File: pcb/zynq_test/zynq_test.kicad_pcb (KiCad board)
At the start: 2 copper layers, 1 part, among them U1 XC7Z020-2CLG400I

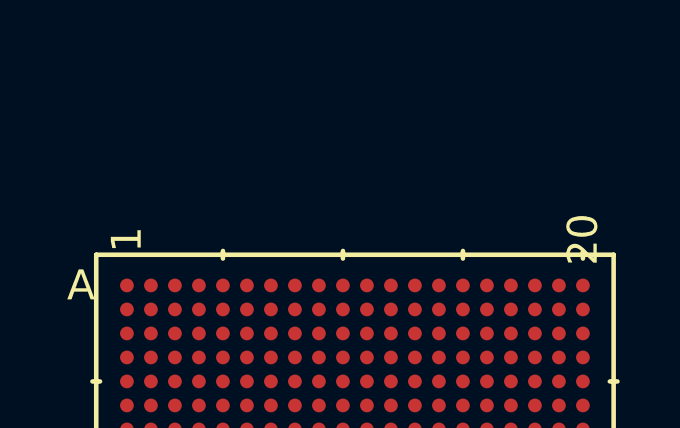
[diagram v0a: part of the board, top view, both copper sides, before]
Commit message: Changed MIO signals to Buses
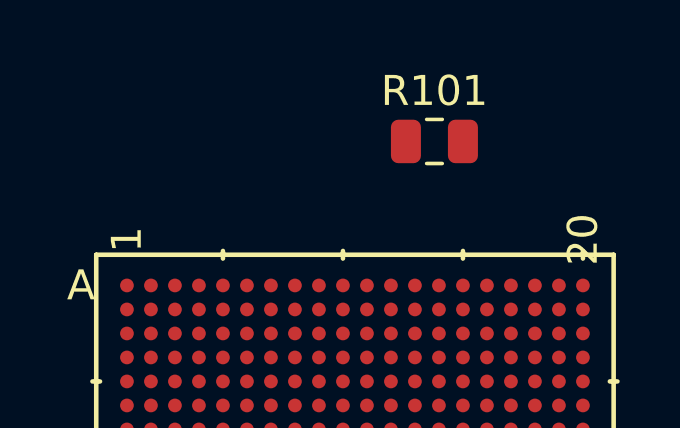
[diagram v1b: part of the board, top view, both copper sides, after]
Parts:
- added R101: R, Capacitor_SMD:C_0805_2012Metric, F.Cu at (137.6, 107.0)
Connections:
- net ETH0-MDC renamed /zynqMio/ETH0-MDC
- net ETH0-MDIO renamed /zynqMio/ETH0-MDIO
- net ETH0-RX-CLK renamed /zynqMio/ETH0-RX-CLK
- net ETH0-RX-CTL renamed /zynqMio/ETH0-RX-CTL
- net ETH0-RXD-0 renamed /zynqMio/ETH0-RXD-0
- net ETH0-RXD-1 renamed /zynqMio/ETH0-RXD-1
- net ETH0-RXD-2 renamed /zynqMio/ETH0-RXD-2
- net ETH0-RXD-3 renamed /zynqMio/ETH0-RXD-3
- net ETH0-TX-CLK renamed /zynqMio/ETH0-TX-CLK
- net ETH0-TX-CTL renamed /zynqMio/ETH0-TX-CTL
- net ETH0-TXD-0 renamed /zynqMio/ETH0-TXD-0
- net ETH0-TXD-1 renamed /zynqMio/ETH0-TXD-1
- net ETH0-TXD-2 renamed /zynqMio/ETH0-TXD-2
- net ETH0-TXD-3 renamed /zynqMio/ETH0-TXD-3
- net MIO0-2 renamed MIO0-8
- net MIO0-3 renamed MIO0-9
- net MIO0-4 renamed MIO0-10
- net MIO0-5 renamed MIO0-11
- net MIO0-6 renamed MIO0-12
- net MIO1-0 renamed /zynqMio/MIO1-46
- net MIO1-1 renamed /zynqMio/MIO1-47
- net MIO1-2 renamed /zynqMio/MIO1-48
- net MIO1-3 renamed /zynqMio/MIO1-49
- net MIO1-4 renamed /zynqMio/MIO1-50
- net MIO1-5 renamed /zynqMio/MIO1-51
- net QSPI0-IO-0/MODE-0 renamed QSPI0-IO-0
- net QSPI0-IO-1/MODE-1 renamed QSPI0-IO-1
- net QSPI0-IO-2/MODE-2 renamed QSPI0-IO-2
- net QSPI0-IO-3/MODE-3 renamed QSPI0-IO-3
- net QSPI0-SCLK/MODE-4 renamed QSPI0-SCLK
- net SD0-CLK renamed /zynqMio/SD0-CLK
- net SD0-CMD renamed /zynqMio/SD0-CMD
- net SD0-DATA-0 renamed /zynqMio/SD0-DATA-0
- net SD0-DATA-1 renamed /zynqMio/SD0-DATA-1
- net SD0-DATA-2 renamed /zynqMio/SD0-DATA-2
- net SD0-DATA-3 renamed /zynqMio/SD0-DATA-3
- net USB0-CLK renamed /zynqMio/USB0-CLK
- net USB0-DATA-0 renamed /zynqMio/USB0-DATA-0
- net USB0-DATA-1 renamed /zynqMio/USB0-DATA-1
- net USB0-DATA-2 renamed /zynqMio/USB0-DATA-2
- net USB0-DATA-3 renamed /zynqMio/USB0-DATA-3
- net USB0-DATA-4 renamed /zynqMio/USB0-DATA-4
- net USB0-DATA-5 renamed /zynqMio/USB0-DATA-5
- net USB0-DATA-6 renamed /zynqMio/USB0-DATA-6
- net USB0-DATA-7 renamed /zynqMio/USB0-DATA-7
- net USB0-DIR renamed /zynqMio/USB0-DIR
- net USB0-NXT renamed /zynqMio/USB0-NXT
- net USB0-STP renamed /zynqMio/USB0-STP
- U1 pad D8: MIO0-1 -> MIO0-7
- U1 pad E11: unconnected-(U1F-PS_MIO_VREF_501-PadE11) -> /zynqMio/0.9_Vref
- U1 pad E8: MIO0-7 -> MIO0-13

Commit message: Finished PS, started on PWR
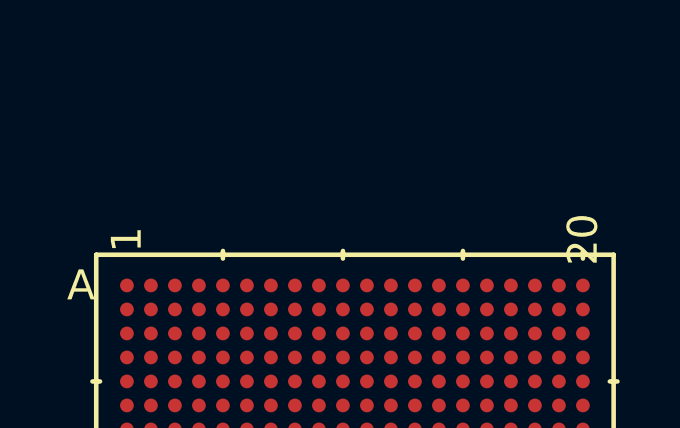
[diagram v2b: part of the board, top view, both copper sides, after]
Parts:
- removed R101: R, Capacitor_SMD:C_0805_2012Metric
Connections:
- net /zynqMio/CLK-33.33M renamed /zynqMio/PS-CLK-33.33M
- net /zynqMio/ETH0-MDC renamed /zynqMio/ETH0.MDC
- net /zynqMio/ETH0-MDIO renamed /zynqMio/ETH0.MDIO
- net /zynqMio/ETH0-RX-CLK renamed /zynqMio/ETH0.RX-CLK
- net /zynqMio/ETH0-RX-CTL renamed /zynqMio/ETH0.RX-CTL
- net /zynqMio/ETH0-RXD-0 renamed /zynqMio/ETH0.RXD-0
- net /zynqMio/ETH0-RXD-1 renamed /zynqMio/ETH0.RXD-1
- net /zynqMio/ETH0-RXD-2 renamed /zynqMio/ETH0.RXD-2
- net /zynqMio/ETH0-RXD-3 renamed /zynqMio/ETH0.RXD-3
- net /zynqMio/ETH0-TX-CLK renamed /zynqMio/ETH0.TX-CLK.Z
- net /zynqMio/ETH0-TX-CTL renamed /zynqMio/ETH0.TX-CTL
- net /zynqMio/ETH0-TXD-0 renamed /zynqMio/ETH0.TXD-0.Z
- net /zynqMio/ETH0-TXD-1 renamed /zynqMio/ETH0.TXD-1.Z
- net /zynqMio/ETH0-TXD-2 renamed /zynqMio/ETH0.TXD-2.Z
- net /zynqMio/ETH0-TXD-3 renamed /zynqMio/ETH0.TXD-3.Z
- net /zynqMio/MIO1-46 renamed /zynqMio/MIO1.46
- net /zynqMio/MIO1-47 renamed /zynqMio/MIO1.47
- net /zynqMio/MIO1-48 renamed /zynqMio/MIO1.48
- net /zynqMio/MIO1-49 renamed /zynqMio/MIO1.49
- net /zynqMio/MIO1-50 renamed /zynqMio/MIO1.50
- net /zynqMio/MIO1-51 renamed /zynqMio/MIO1.51
- net /zynqMio/SD0-CLK renamed /zynqMio/SD0.CLK
- net /zynqMio/SD0-CMD renamed /zynqMio/SD0.CMD
- net /zynqMio/SD0-DATA-0 renamed /zynqMio/SD0.DATA-0
- net /zynqMio/SD0-DATA-1 renamed /zynqMio/SD0.DATA-1
- net /zynqMio/SD0-DATA-2 renamed /zynqMio/SD0.DATA-2
- net /zynqMio/SD0-DATA-3 renamed /zynqMio/SD0.DATA-3
- net /zynqMio/USB0-CLK renamed /zynqMio/USB0.CLK
- net /zynqMio/USB0-DATA-0 renamed /zynqMio/USB0.DATA-0
- net /zynqMio/USB0-DATA-1 renamed /zynqMio/USB0.DATA-1
- net /zynqMio/USB0-DATA-2 renamed /zynqMio/USB0.DATA-2
- net /zynqMio/USB0-DATA-3 renamed /zynqMio/USB0.DATA-3
- net /zynqMio/USB0-DATA-4 renamed /zynqMio/USB0.DATA-4
- net /zynqMio/USB0-DATA-5 renamed /zynqMio/USB0.DATA-5
- net /zynqMio/USB0-DATA-6 renamed /zynqMio/USB0.DATA-6
- net /zynqMio/USB0-DATA-7 renamed /zynqMio/USB0.DATA-7
- net /zynqMio/USB0-DIR renamed /zynqMio/USB0.DIR
- net /zynqMio/USB0-NXT renamed /zynqMio/USB0.NXT
- net /zynqMio/USB0-STP renamed /zynqMio/USB0.STP
- net MIO0-0 renamed /zynqMio/MIO0.0
- net MIO0-10 renamed /zynqMio/MIO0.10
- net MIO0-11 renamed /zynqMio/MIO0.11
- net MIO0-12 renamed /zynqMio/MIO0.12
- net MIO0-13 renamed /zynqMio/MIO0.13
- net MIO0-7 renamed /zynqMio/MIO0.7
- net MIO0-8 renamed /zynqMio/MIO0.8
- net MIO0-9 renamed /zynqMio/MIO0.9
- net QSPI0-IO-0 renamed /zynqMio/QSPI0.IO-0
- net QSPI0-IO-1 renamed /zynqMio/QSPI0.IO-1
- net QSPI0-IO-2 renamed /zynqMio/QSPI0.IO-2
- net QSPI0-IO-3 renamed /zynqMio/QSPI0.IO-3
- net QSPI0-SCLK renamed /zynqMio/QSPI0.SCLK.Z
- net QSPI0-SS-B renamed /zynqMio/QSPI0.SS-B
- net UART0-RX renamed /zynqMio/UART0.RX
- net UART0-TX renamed /zynqMio/UART0.TX
- U1 pad A18: unconnected-(U1H-GND-PadA18) -> GND
- U1 pad A8: unconnected-(U1H-GND-PadA8) -> GND
- U1 pad B1: unconnected-(U1H-GND-PadB1) -> GND
- U1 pad B10: (no net) -> unconnected-(U1A-PS_SRST_B_501-PadB10)
- U1 pad B11: unconnected-(U1H-GND-PadB11) -> GND
- U1 pad C14: unconnected-(U1H-GND-PadC14) -> GND
- U1 pad C4: unconnected-(U1H-GND-PadC4) -> GND
- U1 pad C7: (no net) -> unconnected-(U1A-PS_POR_B_500-PadC7)
- U1 pad C9: unconnected-(U1H-GND-PadC9) -> GND
- U1 pad D17: unconnected-(U1H-GND-PadD17) -> GND
- U1 pad E10: unconnected-(U1H-GND-PadE10) -> GND
- U1 pad E20: unconnected-(U1H-GND-PadE20) -> GND
- U1 pad F11: unconnected-(U1A-VCCBATT_0-PadF11) -> GND
- U1 pad F3: unconnected-(U1H-GND-PadF3) -> GND
- U1 pad F7: unconnected-(U1H-GND-PadF7) -> GND
- U1 pad F8: unconnected-(U1H-VCCPAUX-PadF8) -> Net-(C519-Pad1)
- U1 pad G10: unconnected-(U1H-GND-PadG10) -> GND
- U1 pad G11: unconnected-(U1H-VCCBRAM-PadG11) -> Net-(C508-Pad1)
- U1 pad G12: unconnected-(U1H-GND-PadG12) -> GND
- U1 pad G13: unconnected-(U1H-VCCINT-PadG13) -> Net-(C501-Pad1)
- U1 pad G16: unconnected-(U1H-GND-PadG16) -> GND
- U1 pad G7: unconnected-(U1H-VCCPINT-PadG7) -> Net-(C514-Pad1)
- U1 pad G8: unconnected-(U1H-VCCPLL-PadG8) -> Net-(U1H-VCCPLL)
- U1 pad G9: unconnected-(U1H-VCCPAUX-PadG9) -> Net-(C519-Pad1)
- U1 pad H10: unconnected-(U1H-VCCBRAM-PadH10) -> Net-(C508-Pad1)
- U1 pad H11: unconnected-(U1H-GND-PadH11) -> GND
- U1 pad H12: unconnected-(U1H-VCCINT-PadH12) -> Net-(C501-Pad1)
- U1 pad H13: unconnected-(U1H-GND-PadH13) -> GND
- U1 pad H19: unconnected-(U1H-GND-PadH19) -> GND
- U1 pad H7: unconnected-(U1H-GND-PadH7) -> GND
- U1 pad H8: unconnected-(U1H-VCCPAUX-PadH8) -> Net-(C519-Pad1)
- U1 pad H9: unconnected-(U1H-GND-PadH9) -> GND
- U1 pad J11: unconnected-(U1H-VCCAUX-PadJ11) -> Net-(C511-Pad1)
- U1 pad J12: unconnected-(U1H-GND-PadJ12) -> GND
- U1 pad J13: unconnected-(U1H-VCCINT-PadJ13) -> Net-(C501-Pad1)
- U1 pad J2: unconnected-(U1H-GND-PadJ2) -> GND
- U1 pad J7: unconnected-(U1H-VCCPINT-PadJ7) -> Net-(C514-Pad1)
- U1 pad J8: unconnected-(U1H-GND-PadJ8) -> GND
- U1 pad K11: unconnected-(U1H-GND-PadK11) -> GND
- U1 pad K12: unconnected-(U1H-VCCINT-PadK12) -> Net-(C501-Pad1)
- U1 pad K13: unconnected-(U1H-GND-PadK13) -> GND
- U1 pad K15: unconnected-(U1H-GND-PadK15) -> GND
- U1 pad K5: unconnected-(U1H-GND-PadK5) -> GND
- U1 pad K6: unconnected-(U1A-VCCO_0-PadK6) -> Net-(U1H-VCCO_0)
- U1 pad K7: unconnected-(U1H-GND-PadK7) -> GND
- U1 pad K8: unconnected-(U1H-VCCPAUX-PadK8) -> Net-(C519-Pad1)
- U1 pad L11: unconnected-(U1H-VCCAUX-PadL11) -> Net-(C511-Pad1)
- U1 pad L12: unconnected-(U1H-GND-PadL12) -> GND
- U1 pad L13: unconnected-(U1H-VCCINT-PadL13) -> Net-(C501-Pad1)
- U1 pad L18: unconnected-(U1H-GND-PadL18) -> GND
- U1 pad L7: unconnected-(U1H-VCCPINT-PadL7) -> Net-(C514-Pad1)
- U1 pad L8: unconnected-(U1H-GND-PadL8) -> GND
- U1 pad M1: unconnected-(U1H-GND-PadM1) -> GND
- U1 pad M11: unconnected-(U1H-GND-PadM11) -> GND
- U1 pad M12: unconnected-(U1H-VCCINT-PadM12) -> Net-(C501-Pad1)
- U1 pad M13: unconnected-(U1H-GND-PadM13) -> GND
- U1 pad M7: unconnected-(U1H-GND-PadM7) -> GND
- U1 pad M8: unconnected-(U1H-VCCPAUX-PadM8) -> Net-(C519-Pad1)
- U1 pad N10: unconnected-(U1H-GND-PadN10) -> GND
- U1 pad N11: unconnected-(U1H-VCCAUX-PadN11) -> Net-(C511-Pad1)
- U1 pad N12: unconnected-(U1H-GND-PadN12) -> GND
- U1 pad N13: unconnected-(U1H-VCCINT-PadN13) -> Net-(C501-Pad1)
- U1 pad N14: unconnected-(U1H-GND-PadN14) -> GND
- U1 pad N4: unconnected-(U1H-GND-PadN4) -> GND
- U1 pad N7: unconnected-(U1H-VCCPINT-PadN7) -> Net-(C514-Pad1)
- U1 pad N8: unconnected-(U1H-GND-PadN8) -> GND
- U1 pad N9: unconnected-(U1H-VCCAUX-PadN9) -> Net-(C511-Pad1)
- U1 pad P10: unconnected-(U1H-VCCAUX-PadP10) -> Net-(C511-Pad1)
- U1 pad P11: unconnected-(U1H-GND-PadP11) -> GND
- U1 pad P12: unconnected-(U1H-VCCINT-PadP12) -> Net-(C501-Pad1)
- U1 pad P13: unconnected-(U1H-GND-PadP13) -> GND
- U1 pad P17: unconnected-(U1H-GND-PadP17) -> GND
- U1 pad P7: unconnected-(U1H-GND-PadP7) -> GND
- U1 pad P8: unconnected-(U1H-VCCPINT-PadP8) -> Net-(C514-Pad1)
- U1 pad P9: unconnected-(U1H-GND-PadP9) -> GND
- U1 pad R12: unconnected-(U1H-GND-PadR12) -> GND
- U1 pad R13: unconnected-(U1H-VCCINT-PadR13) -> Net-(C501-Pad1)
- U1 pad R20: unconnected-(U1H-GND-PadR20) -> GND
- U1 pad R7: unconnected-(U1H-VCCPINT-PadR7) -> Net-(C514-Pad1)
- U1 pad R8: unconnected-(U1H-GND-PadR8) -> GND
- U1 pad R9: unconnected-(U1H-VCCAUX-PadR9) -> Net-(C511-Pad1)
- U1 pad T13: unconnected-(U1H-GND-PadT13) -> GND
- U1 pad T3: unconnected-(U1H-GND-PadT3) -> GND
- U1 pad T7: unconnected-(U1H-GND-PadT7) -> GND
- U1 pad U16: unconnected-(U1H-GND-PadU16) -> GND
- U1 pad U6: unconnected-(U1H-GND-PadU6) -> GND
- U1 pad V19: unconnected-(U1H-GND-PadV19) -> GND
- U1 pad V9: unconnected-(U1H-GND-PadV9) -> GND
- U1 pad W12: unconnected-(U1H-GND-PadW12) -> GND
- U1 pad W2: unconnected-(U1H-GND-PadW2) -> GND
- U1 pad Y15: unconnected-(U1H-GND-PadY15) -> GND
- U1 pad Y5: unconnected-(U1H-GND-PadY5) -> GND

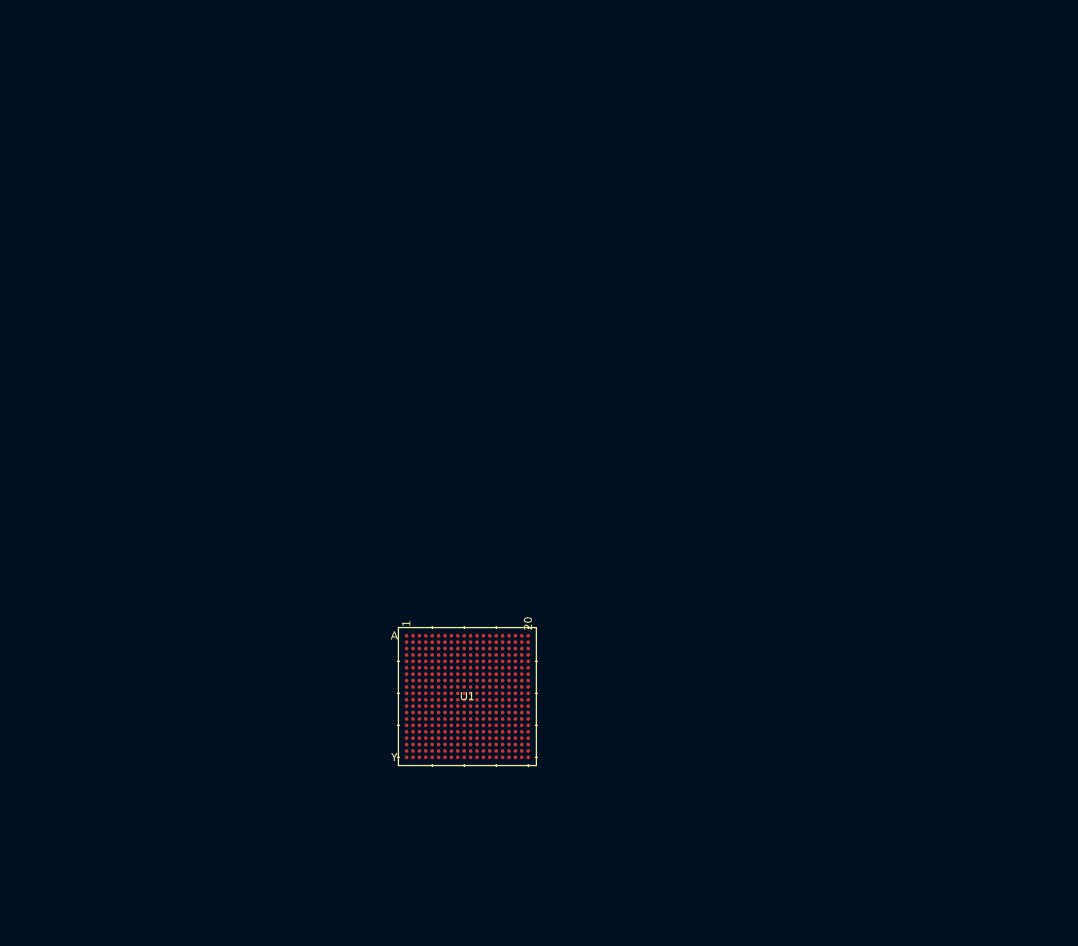
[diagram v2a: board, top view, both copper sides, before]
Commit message: Finished Ethernet, swapped FTDI chip for QFN
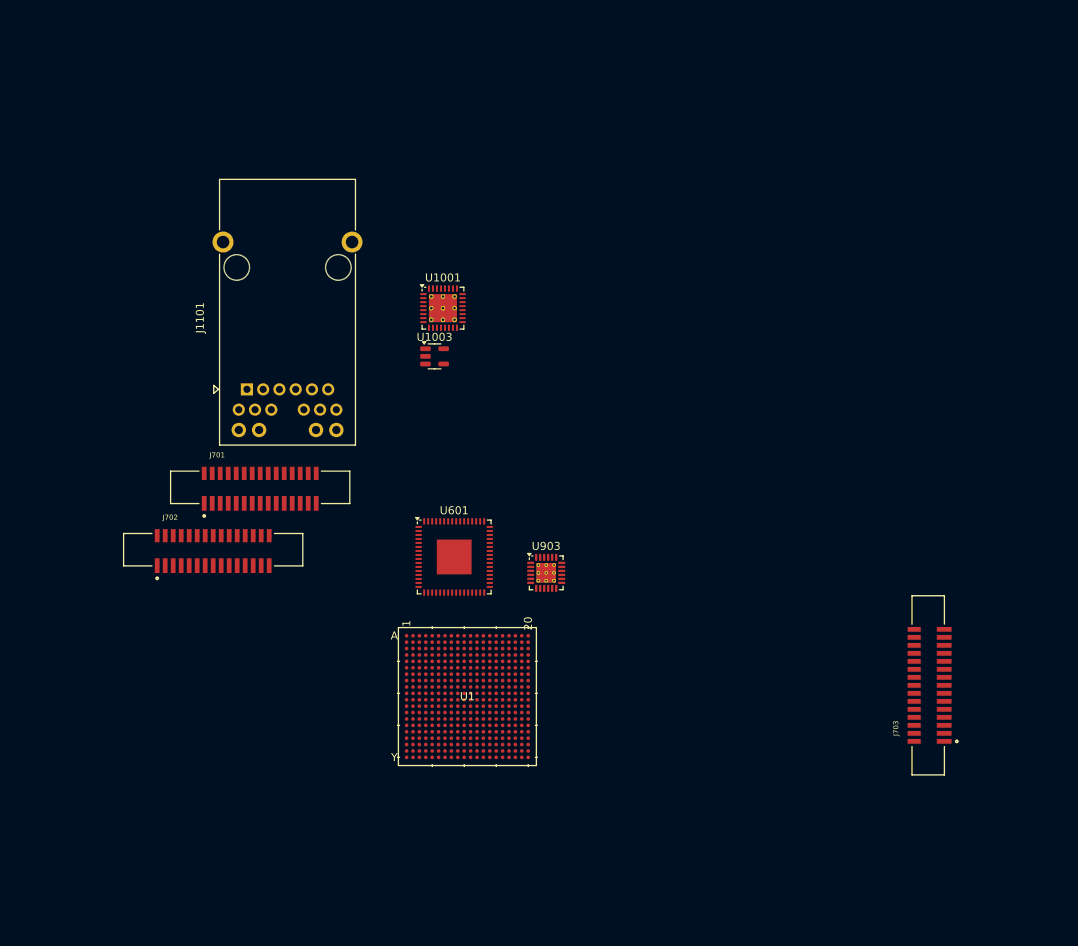
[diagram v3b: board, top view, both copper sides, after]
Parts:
- added J1101: RJ45_JK0654219, Connector_RJ:RJ45_Pulse_JK0654219NL_Horizontal, F.Cu at (107.3, 81.0)
- added J701: 1-1734248-5, Camera:TE_1-1734248-5, F.Cu at (109.0, 93.2)
- added J702: 1-1734248-5, Camera:TE_1-1734248-5, F.Cu at (103.1, 101.0)
- added J703: 1-1734248-5, Camera:TE_1-1734248-5, F.Cu at (192.5, 118.0)
- added U1001: TUSB1210-Q1, Package_DFN_QFN:VQFN-32-1EP_5x5mm_P0.5mm_EP3.5x3.5mm_ThermalVias, F.Cu at (131.8, 70.8)
- added U1003: AP22816AKBWT, Package_TO_SOT_SMD:SOT-23-5, F.Cu at (130.8, 76.9)
- added U601: FT2232HQ, Package_DFN_QFN:QFN-64-1EP_9x9mm_P0.5mm_EP4.35x4.35mm, F.Cu at (133.2, 102.0)
- added U903: TXS02612RTW, Package_DFN_QFN:WQFN-24-1EP_4x4mm_P0.5mm_EP2.45x2.45mm_ThermalVias, F.Cu at (144.8, 103.9)
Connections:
- net /zynqMio/ETH0.TX-CTL renamed /zynqMio/ETH0.TX-CTL.Z
- net /zynqMio/QSPI0.IO-0 renamed /Boot/QSPI0.IO-0
- net /zynqMio/QSPI0.IO-1 renamed /Boot/QSPI0.IO-1
- net /zynqMio/QSPI0.IO-2 renamed /Boot/QSPI0.IO-2
- net /zynqMio/QSPI0.IO-3 renamed /Boot/QSPI0.IO-3
- net /zynqMio/QSPI0.SS-B renamed /Boot/QSPI0.SS-B
- net /zynqMio/SD0.CLK renamed /zynqMio/SD0.CLK.Z
- net /zynqMio/USB0.CLK renamed /USB_OTG/USB0.CLK
- net Net-(U1H-VCCPLL) renamed /ZynqPWR+JTAG/VCC_PLL
- U1 pad A10: /zynqMio/USB0.DATA-5 -> /USB_OTG/USB0.DATA-5
- U1 pad A12: /zynqMio/USB0.DATA-2 -> /USB_OTG/USB0.DATA-2
- U1 pad A14: /zynqMio/USB0.DATA-0 -> /USB_OTG/USB0.DATA-0
- U1 pad A2: unconnected-(U1G-PS_DDR_DQ2_502-PadA2) -> /ZynqDram/DDR_L0.2
- U1 pad A3: unconnected-(U1G-VCCO_DDR_502-PadA3) -> Net-(C517-Pad1)
- U1 pad A4: unconnected-(U1G-PS_DDR_DQ3_502-PadA4) -> /ZynqDram/DDR_L0.3
- U1 pad A9: /zynqMio/SD0.DATA-1 -> /Boot/SD0.DATA-1
- U1 pad B10: unconnected-(U1A-PS_SRST_B_501-PadB10) -> /ZynqPWR+JTAG/PS_RST
- U1 pad B15: /zynqMio/SD0.DATA-3 -> /Boot/SD0.DATA-3
- U1 pad B3: unconnected-(U1G-PS_DDR_DQ1_502-PadB3) -> /ZynqDram/DDR_L0.1
- U1 pad C1: unconnected-(U1G-PS_DDR_DQ6_502-PadC1) -> /ZynqDram/DDR_L0.6
- U1 pad C13: /zynqMio/USB0.DIR -> /USB_OTG/USB0.DIR
- U1 pad C15: /zynqMio/USB0.STP -> /USB_OTG/USB0.STP
- U1 pad C16: /zynqMio/USB0.DATA-4 -> /USB_OTG/USB0.DATA-4
- U1 pad C17: /zynqMio/SD0.CMD -> /Boot/SD0.CMD
- U1 pad C18: /zynqMio/USB0.DATA-7 -> /USB_OTG/USB0.DATA-7
- U1 pad C19: unconnected-(U1D-VCCO_35-PadC19) -> Net-(C308-Pad1)
- U1 pad C3: unconnected-(U1G-PS_DDR_DQ0_502-PadC3) -> /ZynqDram/DDR_L0.0
- U1 pad C7: unconnected-(U1A-PS_POR_B_500-PadC7) -> /ZynqPWR+JTAG/PWR_ON_RST
- U1 pad D1: unconnected-(U1G-PS_DDR_DQ5_502-PadD1) -> /ZynqDram/DDR_L0.5
- U1 pad D15: /zynqMio/USB0.DATA-1 -> /USB_OTG/USB0.DATA-1
- U1 pad D2: unconnected-(U1G-VCCO_DDR_502-PadD2) -> Net-(C517-Pad1)
- U1 pad D3: unconnected-(U1G-PS_DDR_DQ4_502-PadD3) -> /ZynqDram/DDR_L0.4
- U1 pad E1: unconnected-(U1G-PS_DDR_DQ7_502-PadE1) -> /ZynqDram/DDR_L0.7
- U1 pad E12: /zynqMio/SD0.DATA-0 -> /Boot/SD0.DATA-0
- U1 pad E13: /zynqMio/USB0.DATA-6 -> /USB_OTG/USB0.DATA-6
- U1 pad E16: /zynqMio/USB0.NXT -> /USB_OTG/USB0.NXT
- U1 pad E2: unconnected-(U1G-PS_DDR_DQ8_502-PadE2) -> /ZynqDram/DDR_L0.8
- U1 pad E3: unconnected-(U1G-PS_DDR_DQ9_502-PadE3) -> /ZynqDram/DDR_L1.9
- U1 pad E5: unconnected-(U1G-VCCO_DDR_502-PadE5) -> Net-(C517-Pad1)
- U1 pad F10: unconnected-(U1A-RSVDGND-PadF10) -> GND
- U1 pad F12: /zynqMio/USB0.DATA-3 -> /USB_OTG/USB0.DATA-3
- U1 pad F13: /zynqMio/SD0.DATA-2 -> /Boot/SD0.DATA-2
- U1 pad F18: unconnected-(U1D-VCCO_35-PadF18) -> Net-(C308-Pad1)
- U1 pad F6: unconnected-(U1A-TDO_0-PadF6) -> /Programmer/JTAG.Z.TDO
- U1 pad F8: Net-(C519-Pad1) -> +1V8
- U1 pad F9: unconnected-(U1A-TCK_0-PadF9) -> /Programmer/JTAG.Z.CLK
- U1 pad G1: unconnected-(U1G-VCCO_DDR_502-PadG1) -> Net-(C517-Pad1)
- U1 pad G11: Net-(C508-Pad1) -> +1V0
- U1 pad G13: Net-(C501-Pad1) -> +1V0
- U1 pad G3: unconnected-(U1G-PS_DDR_DQ10_502-PadG3) -> /ZynqDram/DDR_L1.10
- U1 pad G6: unconnected-(U1A-TDI_0-PadG6) -> /Programmer/JTAG.Z.TDI
- U1 pad G7: Net-(C514-Pad1) -> +1V0
- U1 pad G9: Net-(C519-Pad1) -> +1V8
- U1 pad H1: unconnected-(U1G-PS_DDR_DQ14_502-PadH1) -> /ZynqDram/DDR_L1.14
- U1 pad H10: Net-(C508-Pad1) -> +1V0
- U1 pad H12: Net-(C501-Pad1) -> +1V0
- U1 pad H14: unconnected-(U1D-VCCO_35-PadH14) -> Net-(C308-Pad1)
- U1 pad H2: unconnected-(U1G-PS_DDR_DQ13_502-PadH2) -> /ZynqDram/DDR_L1.13
- U1 pad H3: unconnected-(U1G-PS_DDR_DQ11_502-PadH3) -> /ZynqDram/DDR_L1.11
- U1 pad H4: unconnected-(U1G-VCCO_DDR_502-PadH4) -> Net-(C517-Pad1)
- U1 pad H8: Net-(C519-Pad1) -> +1V8
- U1 pad J1: unconnected-(U1G-PS_DDR_DQ15_502-PadJ1) -> /ZynqDram/DDR_L1.15
- U1 pad J10: unconnected-(U1A-GNDADC_0-PadJ10) -> GND
- U1 pad J11: Net-(C511-Pad1) -> +1V8
- U1 pad J13: Net-(C501-Pad1) -> +1V0
- U1 pad J17: unconnected-(U1D-VCCO_35-PadJ17) -> Net-(C308-Pad1)
- U1 pad J3: unconnected-(U1G-PS_DDR_DQ12_502-PadJ3) -> /ZynqDram/DDR_L1.12
- U1 pad J6: unconnected-(U1A-TMS_0-PadJ6) -> /Programmer/JTAG.Z.TMS
- U1 pad J7: Net-(C514-Pad1) -> +1V0
- U1 pad J9: unconnected-(U1A-VCCADC_0-PadJ9) -> +1V8
- U1 pad K10: unconnected-(U1A-VREFN_0-PadK10) -> GND
- U1 pad K12: Net-(C501-Pad1) -> +1V0
- U1 pad K20: unconnected-(U1D-VCCO_35-PadK20) -> Net-(C308-Pad1)
- U1 pad K6: Net-(U1H-VCCO_0) -> +3.3V
- U1 pad K8: Net-(C519-Pad1) -> +1V8
- U1 pad K9: unconnected-(U1A-VP_0-PadK9) -> /ZynqPWR+JTAG/XADC_0
- U1 pad L10: unconnected-(U1A-VN_0-PadL10) -> GND
- U1 pad L11: Net-(C511-Pad1) -> +1V8
- U1 pad L13: Net-(C501-Pad1) -> +1V0
- U1 pad L3: unconnected-(U1G-VCCO_DDR_502-PadL3) -> Net-(C517-Pad1)
- U1 pad L6: unconnected-(U1A-PROGRAM_B_0-PadL6) -> /ZynqPWR+JTAG/PROG
- U1 pad L7: Net-(C514-Pad1) -> +1V0
- U1 pad L9: unconnected-(U1A-VREFP_0-PadL9) -> GND
- U1 pad M10: unconnected-(U1A-DXN_0-PadM10) -> GND
- U1 pad M12: Net-(C501-Pad1) -> +1V0
- U1 pad M16: unconnected-(U1D-VCCO_35-PadM16) -> Net-(C308-Pad1)
- U1 pad M6: unconnected-(U1A-CFGBVS_0-PadM6) -> +3.3V
- U1 pad M8: Net-(C519-Pad1) -> +1V8
- U1 pad M9: unconnected-(U1A-DXP_0-PadM9) -> GND
- U1 pad N11: Net-(C511-Pad1) -> +1V8
- U1 pad N13: Net-(C501-Pad1) -> +1V0
- U1 pad N19: unconnected-(U1C-VCCO_34-PadN19) -> Net-(C315-Pad1)
- U1 pad N6: unconnected-(U1A-RSVDVCC3-PadN6) -> +3.3V
- U1 pad N7: Net-(C514-Pad1) -> +1V0
- U1 pad N9: Net-(C511-Pad1) -> +1V8
- U1 pad P1: unconnected-(U1G-PS_DDR_DQ16_502-PadP1) -> /ZynqDram/DDR_L1.16
- U1 pad P10: Net-(C511-Pad1) -> +1V8
- U1 pad P12: Net-(C501-Pad1) -> +1V0
- U1 pad P2: unconnected-(U1G-VCCO_DDR_502-PadP2) -> Net-(C517-Pad1)
- U1 pad P3: unconnected-(U1G-PS_DDR_DQ17_502-PadP3) -> /ZynqDram/DDR_L2.17
- U1 pad P8: Net-(C514-Pad1) -> +1V0
- U1 pad R1: unconnected-(U1G-PS_DDR_DQ19_502-PadR1) -> /ZynqDram/DDR_L2.19
- U1 pad R10: unconnected-(U1A-INIT_B_0-PadR10) -> /ZynqPWR+JTAG/INIT
- U1 pad R11: unconnected-(U1A-DONE_0-PadR11) -> /ZynqPWR+JTAG/DONE
- U1 pad R13: Net-(C501-Pad1) -> +1V0
- U1 pad R15: unconnected-(U1C-VCCO_34-PadR15) -> Net-(C315-Pad1)
- U1 pad R3: unconnected-(U1G-PS_DDR_DQ18_502-PadR3) -> /ZynqDram/DDR_L2.18
- U1 pad R5: unconnected-(U1G-VCCO_DDR_502-PadR5) -> Net-(C517-Pad1)
- U1 pad R6: unconnected-(U1A-RSVDVCC2-PadR6) -> +3.3V
- U1 pad R7: Net-(C514-Pad1) -> +1V0
- U1 pad R9: Net-(C511-Pad1) -> +1V8
- U1 pad T18: unconnected-(U1C-VCCO_34-PadT18) -> Net-(C315-Pad1)
- U1 pad T4: unconnected-(U1G-PS_DDR_DQ20_502-PadT4) -> /ZynqDram/DDR_L2.20
- U1 pad T6: unconnected-(U1A-RSVDVCC1-PadT6) -> +3.3V
- U1 pad T8: unconnected-(U1B-VCCO_13-PadT8) -> Net-(C301-Pad1)
- U1 pad U1: unconnected-(U1G-VCCO_DDR_502-PadU1) -> Net-(C517-Pad1)
- U1 pad U11: unconnected-(U1B-VCCO_13-PadU11) -> Net-(C301-Pad1)
- U1 pad U2: unconnected-(U1G-PS_DDR_DQ22_502-PadU2) -> /ZynqDram/DDR_L2.22
- U1 pad U3: unconnected-(U1G-PS_DDR_DQ23_502-PadU3) -> /ZynqDram/DDR_L2.23
- U1 pad U4: unconnected-(U1G-PS_DDR_DQ21_502-PadU4) -> /ZynqDram/DDR_L2.21
- U1 pad V1: unconnected-(U1G-PS_DDR_DQ24_502-PadV1) -> /ZynqDram/DDR_L3.24
- U1 pad V14: unconnected-(U1C-VCCO_34-PadV14) -> Net-(C315-Pad1)
- U1 pad V2: unconnected-(U1G-PS_DDR_DQ30_502-PadV2) -> /ZynqDram/DDR_L3.30
- U1 pad V3: unconnected-(U1G-PS_DDR_DQ31_502-PadV3) -> /ZynqDram/DDR_L3.31
- U1 pad V4: unconnected-(U1G-VCCO_DDR_502-PadV4) -> Net-(C517-Pad1)
- U1 pad W1: unconnected-(U1G-PS_DDR_DQ26_502-PadW1) -> /ZynqDram/DDR_L3.26
- U1 pad W17: unconnected-(U1C-VCCO_34-PadW17) -> Net-(C315-Pad1)
- U1 pad W3: unconnected-(U1G-PS_DDR_DQ29_502-PadW3) -> /ZynqDram/DDR_L3.29
- U1 pad W7: unconnected-(U1B-VCCO_13-PadW7) -> Net-(C301-Pad1)
- U1 pad Y10: unconnected-(U1B-VCCO_13-PadY10) -> Net-(C301-Pad1)
- U1 pad Y2: unconnected-(U1G-PS_DDR_DQ28_502-PadY2) -> /ZynqDram/DDR_L3.28
- U1 pad Y20: unconnected-(U1C-VCCO_34-PadY20) -> Net-(C315-Pad1)
- U1 pad Y3: unconnected-(U1G-PS_DDR_DQ25_502-PadY3) -> /ZynqDram/DDR_L3.25
- U1 pad Y4: unconnected-(U1G-PS_DDR_DQ27_502-PadY4) -> /ZynqDram/DDR_L3.27
